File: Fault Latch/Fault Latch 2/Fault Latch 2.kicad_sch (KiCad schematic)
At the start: 110 parts, among them K101 Fujitsu_FTR-LYAA005x, K102 Fujitsu_FTR-LYAA005x, K103 Fujitsu_FTR-LYAA005x, Q101 Q_NPN_BEC, Q102 Q_NPN_BEC, Q103 Q_NPN_BEC, Q104 Q_NPN_BEC, Q105 Q_NMOS_GSD, Q106 Q_NMOS_GSD, Q107 Q_PMOS_GSD, Q108 Q_PMOS_GSD, Q109 Q_NMOS_GDS, Q110 Q_NPN_BEC, Q111 Q_NPN_BEC, Q112 Q_NMOS_GSD, Q113 Q_PMOS_GSD, Q114 Q_NMOS_GSD, Q115 Q_NMOS_GSD, SW101 SW_Omron_B3FS, SW102 SW_Omron_B3FS, SW103 SW_Omron_B3FS, U101 SFH617A-1, U102 SFH617A-1, U103 SFH617A-1, U104 74AHC1G00, U105 74AHC1G00, U106 74AHC1G00, U107 74LS279, U108 641964-1, U109 SFH617A-1, U110 SFH617A-1, U111 641964-1, U112 641964-1, U113 641964-1, U114 641964-1, U115 641964-1, U116 641964-1, U117 74AHC1G00, U118 LM555xM, U119 74AHC1G00, U120 641964-1, U121 SFH617A-1, U122 641964-1, U123 641964-1

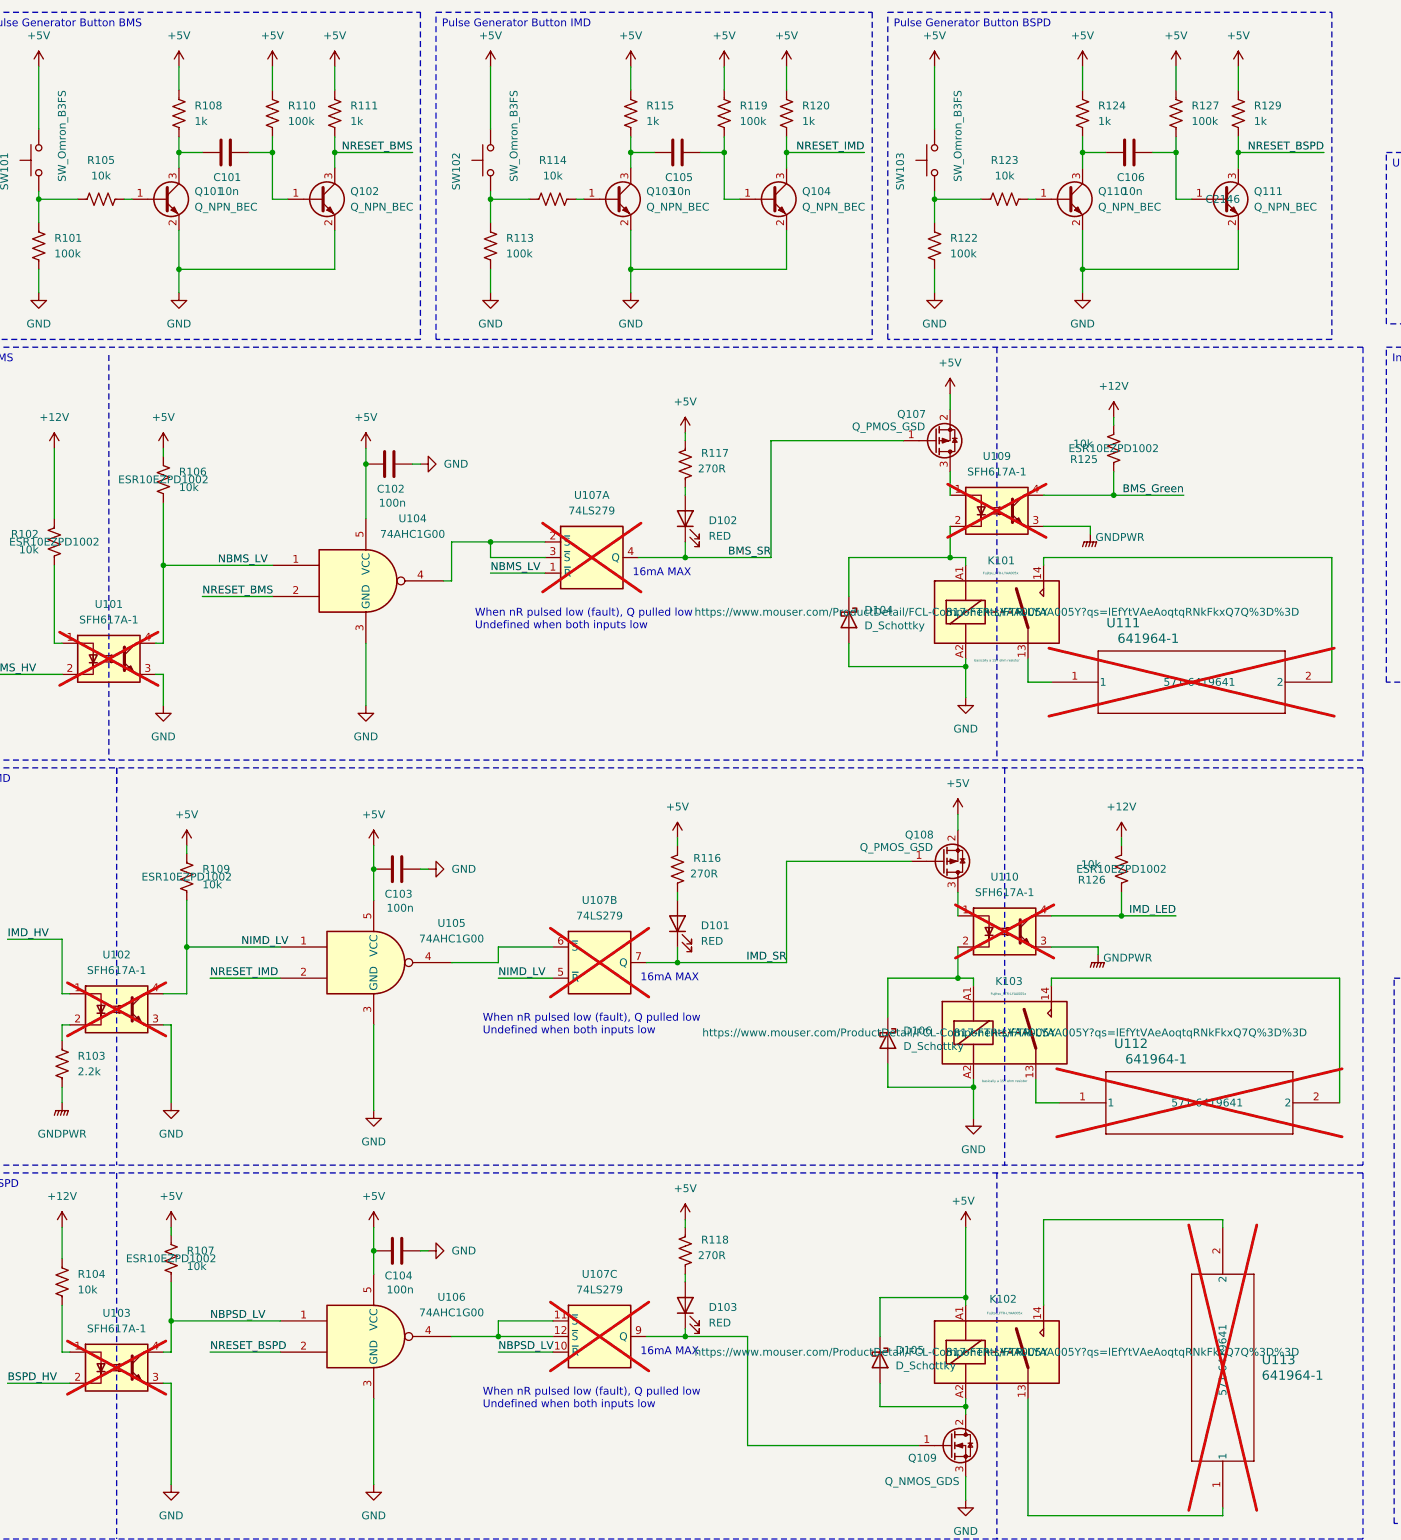
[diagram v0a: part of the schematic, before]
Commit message: Fixed errors on schematic. Need to update pcb layout
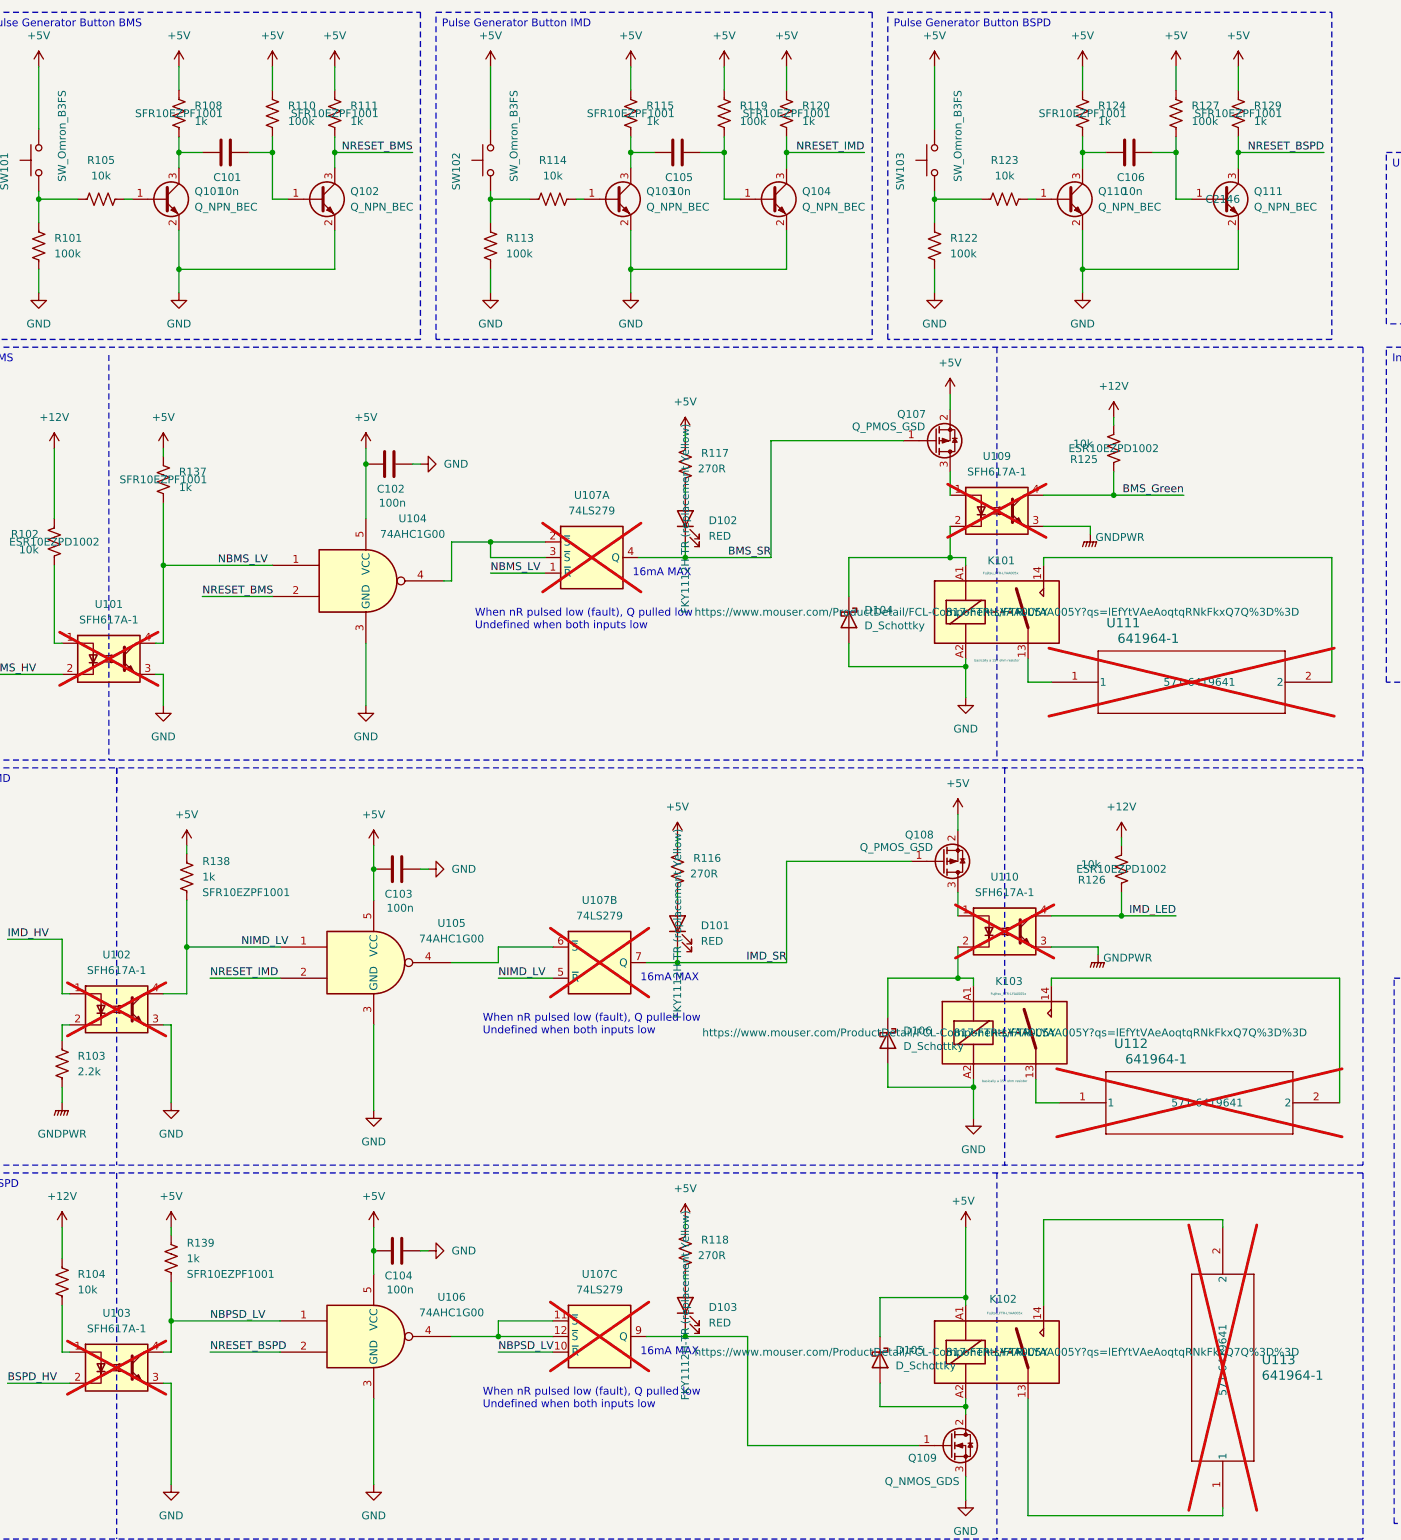
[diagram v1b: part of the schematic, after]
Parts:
- removed R106, R107, R109: 10k, Resistor_SMD:R_0805_2012Metric_Pad1.20x1.40mm_HandSolder, symbol Device:R_US
- added R137, R138, R139: 1k, Resistor_SMD:R_0805_2012Metric_Pad1.20x1.40mm_HandSolder, symbol Device:R_US
- D101, D102, D103: MOUSER (none) -> FKY1112H-TR (replacement Yellow)
- R108, R111, R115, R120, R124, R129: MOUSER (none) -> SFR10EZPF1001
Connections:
- net +5V: now also R137.1, R138.2, R139.2
- net NBMS_LV: now also R137.2
- net NBPSD_LV: now also R139.1
- net NIMD_LV: now also R138.1
